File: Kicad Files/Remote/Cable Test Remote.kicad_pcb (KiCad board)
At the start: 2 copper layers, 25.4 x 95.9 mm, 23 parts, among them J1 RJ45, J2 RJ12

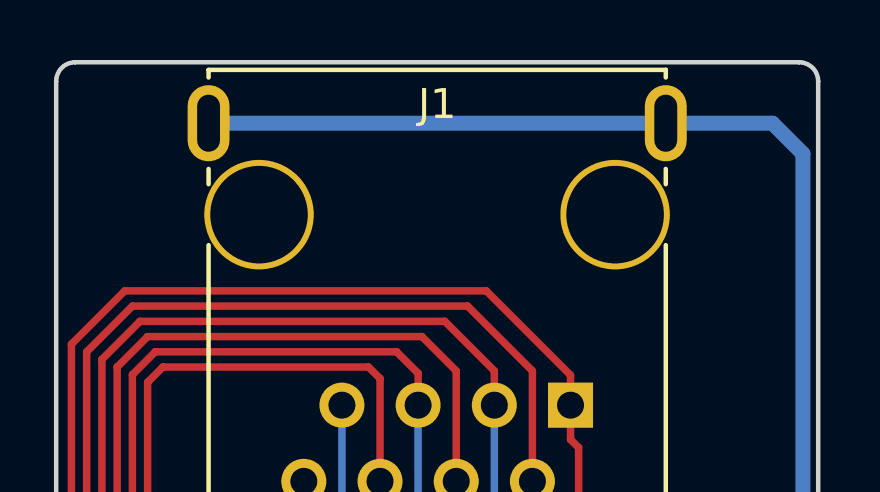
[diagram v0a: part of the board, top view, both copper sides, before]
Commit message: Fix small measurement error in RJ-45 Footprint
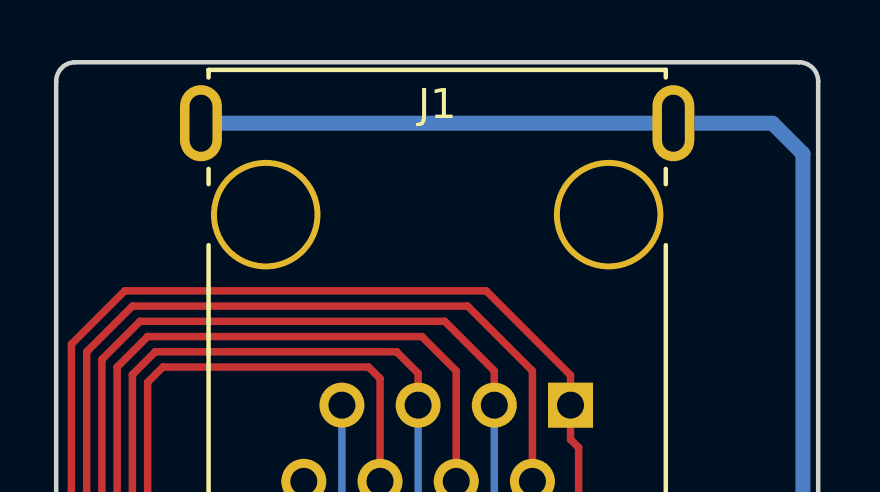
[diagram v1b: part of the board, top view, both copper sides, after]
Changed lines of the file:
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@@
     (add_net "Net-(D1-Pad2)")
-  )
-  (module Tester_Connectors:RJ45_SHLD (layer F.Cu)
-    (at 114.3 55.88 180)
-    (tags RJ45)
-    (fp_text reference J1 (at 0 3.683 180) (layer F.SilkS)
-      (effects (font (size 1 1) (thickness 0.15)))
-    )
-    (fp_text value RJ45 (at 0.14224 -0.1016 180) (layer F.Fab)
-      (effects (font (size 1 1) (thickness 0.15)))
-    )
-    (fp_line (start 7.62 -1.016) (end 7.62 -10.16) (layer F.SilkS) (width 0.15))
-    (fp_line (start 7.62 -10.16) (end -7.62 -10.16) (layer F.SilkS) (width 0.15))
-    (fp_line (start -7.62 -10.16) (end -7.62 -1.016) (layer F.SilkS) (width 0.15))
-    (fp_line (start 7.62 4.572) (end 7.62 4.826) (layer F.SilkS) (width 0.15))
-    (fp_line (start 7.62 4.826) (end -7.62 4.826) (layer F.SilkS) (width 0.15))
-    (fp_line (start -7.62 4.826) (end -7.62 4.572) (layer F.SilkS) (width 0.15))
-    (fp_line (start -7.62 1.524) (end -7.62 1.016) (layer F.SilkS) (width 0.15))
-    (fp_line (start 7.62 1.016) (end 7.62 1.524) (layer F.SilkS) (width 0.15))
-    (pad 9 thru_hole oval (at -7.62 3.048 180) (size 1.397 2.54) (drill oval 0.762 1.905) (layers *.Cu *.Mask F.SilkS)
-      (net 10 /S))
-    (pad "" np_thru_hole circle (at 5.93852 0 180) (size 3.64998 3.64998) (drill 3.2512) (layers *.Cu *.SilkS *.Mask))
-    (pad Hole np_thru_hole circle (at -5.9309 0 180) (size 3.64998 3.64998) (drill 3.2512) (layers *.Cu *.SilkS *.Mask))
-    (pad 1 thru_hole rect (at -4.445 -6.35 180) (size 1.50114 1.50114) (drill 0.89916) (layers *.Cu *.Mask F.SilkS)
-      (net 1 /1))
-    (pad 2 thru_hole circle (at -3.175 -8.89 180) (size 1.50114 1.50114) (drill 0.89916) (layers *.Cu *.Mask F.SilkS)
-      (net 3 /2))
-    (pad 3 thru_hole circle (at -1.905 -6.35 180) (size 1.50114 1.50114) (drill 0.89916) (layers *.Cu *.Mask F.SilkS)
-      (net 4 /3))
-    (pad 4 thru_hole circle (at -0.635 -8.89 180) (size 1.50114 1.50114) (drill 0.89916) (layers *.Cu *.Mask F.SilkS)
-      (net 5 /4))
-    (pad 5 thru_hole circle (at 0.635 -6.35 180) (size 1.50114 1.50114) (drill 0.89916) (layers *.Cu *.Mask F.SilkS)
-      (net 6 /5))
-    (pad 6 thru_hole circle (at 1.905 -8.89 180) (size 1.50114 1.50114) (drill 0.89916) (layers *.Cu *.Mask F.SilkS)
-      (net 7 /6))
-    (pad 7 thru_hole circle (at 3.175 -6.35 180) (size 1.50114 1.50114) (drill 0.89916) (layers *.Cu *.Mask F.SilkS)
-      (net 8 /7))
-    (pad 8 thru_hole circle (at 4.445 -8.89 180) (size 1.50114 1.50114) (drill 0.89916) (layers *.Cu *.Mask F.SilkS)
-      (net 9 /8))
-    (pad 9 thru_hole oval (at 7.62 3.048 180) (size 1.397 2.54) (drill oval 0.762 1.905) (layers *.Cu *.Mask F.SilkS)
-      (net 10 /S))
-    (model Connect.3dshapes/RJ45_8.wrl
-      (at (xyz 0 0 0))
-      (scale (xyz 0.4 0.4 0.4))
-      (rotate (xyz 0 0 0))
-    )
   )
   (module Diodes_SMD:SOD-123 (layer F.Cu)
@@
     (pad "" np_thru_hole circle (at 5.08 0) (size 3.64998 3.64998) (drill 3.2512) (layers *.Cu *.Mask F.SilkS))
     (pad "" np_thru_hole circle (at -5.08 0) (size 3.64998 3.64998) (drill 3.2512) (layers *.Cu *.Mask F.SilkS))
+  )
+  (module Tester_Connectors:RJ45_SHLD (layer F.Cu)
+    (at 114.3 55.88 180)
+    (tags RJ45)
+    (fp_text reference J1 (at 0 3.683 180) (layer F.SilkS)
+      (effects (font (size 1 1) (thickness 0.15)))
+    )
+    (fp_text value RJ45 (at 0.14224 -0.1016 180) (layer F.Fab)
+      (effects (font (size 1 1) (thickness 0.15)))
+    )
+    (fp_line (start 7.62 -1.016) (end 7.62 -10.16) (layer F.SilkS) (width 0.15))
+    (fp_line (start 7.62 -10.16) (end -7.62 -10.16) (layer F.SilkS) (width 0.15))
+    (fp_line (start -7.62 -10.16) (end -7.62 -1.016) (layer F.SilkS) (width 0.15))
+    (fp_line (start 7.62 4.572) (end 7.62 4.826) (layer F.SilkS) (width 0.15))
+    (fp_line (start 7.62 4.826) (end -7.62 4.826) (layer F.SilkS) (width 0.15))
+    (fp_line (start -7.62 4.826) (end -7.62 4.572) (layer F.SilkS) (width 0.15))
+    (fp_line (start -7.62 1.524) (end -7.62 1.016) (layer F.SilkS) (width 0.15))
+    (fp_line (start 7.62 1.016) (end 7.62 1.524) (layer F.SilkS) (width 0.15))
+    (pad 9 thru_hole oval (at -7.874 3.048 180) (size 1.397 2.54) (drill oval 0.762 1.905) (layers *.Cu *.Mask F.SilkS)
+      (net 10 /S))
+    (pad "" np_thru_hole circle (at 5.715 0 180) (size 3.64998 3.64998) (drill 3.2512) (layers *.Cu *.SilkS *.Mask))
+    (pad "" np_thru_hole circle (at -5.715 0 180) (size 3.64998 3.64998) (drill 3.2512) (layers *.Cu *.SilkS *.Mask))
+    (pad 1 thru_hole rect (at -4.445 -6.35 180) (size 1.50114 1.50114) (drill 0.89916) (layers *.Cu *.Mask F.SilkS)
+      (net 1 /1))
+    (pad 2 thru_hole circle (at -3.175 -8.89 180) (size 1.50114 1.50114) (drill 0.89916) (layers *.Cu *.Mask F.SilkS)
+      (net 3 /2))
+    (pad 3 thru_hole circle (at -1.905 -6.35 180) (size 1.50114 1.50114) (drill 0.89916) (layers *.Cu *.Mask F.SilkS)
+      (net 4 /3))
+    (pad 4 thru_hole circle (at -0.635 -8.89 180) (size 1.50114 1.50114) (drill 0.89916) (layers *.Cu *.Mask F.SilkS)
+      (net 5 /4))
+    (pad 5 thru_hole circle (at 0.635 -6.35 180) (size 1.50114 1.50114) (drill 0.89916) (layers *.Cu *.Mask F.SilkS)
+      (net 6 /5))
+    (pad 6 thru_hole circle (at 1.905 -8.89 180) (size 1.50114 1.50114) (drill 0.89916) (layers *.Cu *.Mask F.SilkS)
+      (net 7 /6))
+    (pad 7 thru_hole circle (at 3.175 -6.35 180) (size 1.50114 1.50114) (drill 0.89916) (layers *.Cu *.Mask F.SilkS)
+      (net 8 /7))
+    (pad 8 thru_hole circle (at 4.445 -8.89 180) (size 1.50114 1.50114) (drill 0.89916) (layers *.Cu *.Mask F.SilkS)
+      (net 9 /8))
+    (pad 9 thru_hole oval (at 7.874 3.048 180) (size 1.397 2.54) (drill oval 0.762 1.905) (layers *.Cu *.Mask F.SilkS)
+      (net 10 /S))
+    (model Connect.3dshapes/RJ45_8.wrl
+      (at (xyz 0 0 0))
+      (scale (xyz 0.4 0.4 0.4))
+      (rotate (xyz 0 0 0))
+    )
   )
   (gr_line (start 127 146.05) (end 127 51.435) (layer Edge.Cuts) (width 0.15))
@@
   (segment (start 118.11 100.584) (end 119.015 99.679) (width 0.25) (layer B.Cu) (net 9))
   (segment (start 119.015 99.679) (end 119.015 97.79) (width 0.25) (layer B.Cu) (net 9))
+  (segment (start 122.174 52.832) (end 106.426 52.832) (width 0.5) (layer B.Cu) (net 10))
+  (segment (start 125.476 52.832) (end 122.174 52.832) (width 0.5) (layer B.Cu) (net 10))
   (segment (start 126.492 143.637) (end 126.492 109.22) (width 0.5) (layer B.Cu) (net 10))
-  (segment (start 121.92 52.832) (end 106.68 52.832) (width 0.5) (layer B.Cu) (net 10))
   (segment (start 126.492 109.22) (end 126.492 108.204) (width 0.5) (layer B.Cu) (net 10))
   (segment (start 125.476 109.22) (end 126.492 109.22) (width 0.25) (layer B.Cu) (net 10))
@@
   (segment (start 126.492 53.848) (end 126.492 108.204) (width 0.5) (layer B.Cu) (net 10))
   (segment (start 125.476 52.832) (end 126.492 53.848) (width 0.5) (layer B.Cu) (net 10))
-  (segment (start 121.92 52.832) (end 125.476 52.832) (width 0.5) (layer B.Cu) (net 10))
   (segment (start 113.538 105.156) (end 113.03 105.664) (width 0.25) (layer F.Cu) (net 10))
   (segment (start 113.03 105.664) (end 113.03 107.1372) (width 0.25) (layer F.Cu) (net 10))
